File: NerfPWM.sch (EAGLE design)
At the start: 37 parts, among them IC1 MEGA48/88/168-AU, Q1 MOSFET-NCHANNELSMD, Q2 MOSFET-NCHANNELSMD

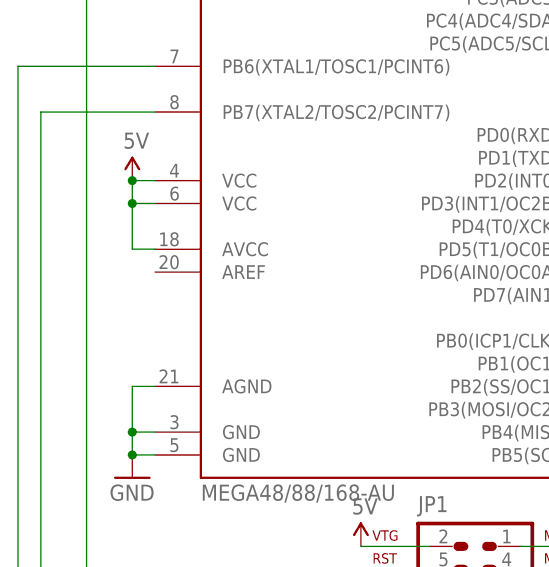
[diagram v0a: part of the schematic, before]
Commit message: Increased spacing around FET ground connections.
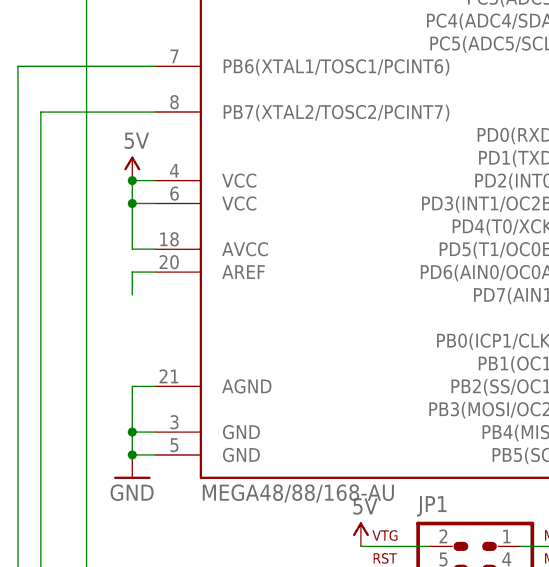
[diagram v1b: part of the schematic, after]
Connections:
- new net N$1: IC1.AREF
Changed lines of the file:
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@@
+</segment>
+</net>
+<net name="N$1" class="0">
+<segment>
+<pinref part="IC1" gate="1" pin="AREF"/>
+<wire x1="-2.54" y1="104.14" x2="-5.08" y2="104.14" width="0.1524" layer="91"/>
+<wire x1="-5.08" y1="104.14" x2="-5.08" y2="101.6" width="0.1524" layer="91"/>
 </segment>
 </net>
